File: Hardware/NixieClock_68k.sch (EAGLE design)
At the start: 47 parts, among them IC1 68008, IC10 7805, IC11 MIC803, IC12 74HC08N, IC2 AS6C1008, IC3 39SF020, IC4 DS1244Y, IC5 68681, IC6 74HC30N, IC7 74HC04N, IC8 74HC138N, IC9 74HC266N, Q1 3.6864MHz

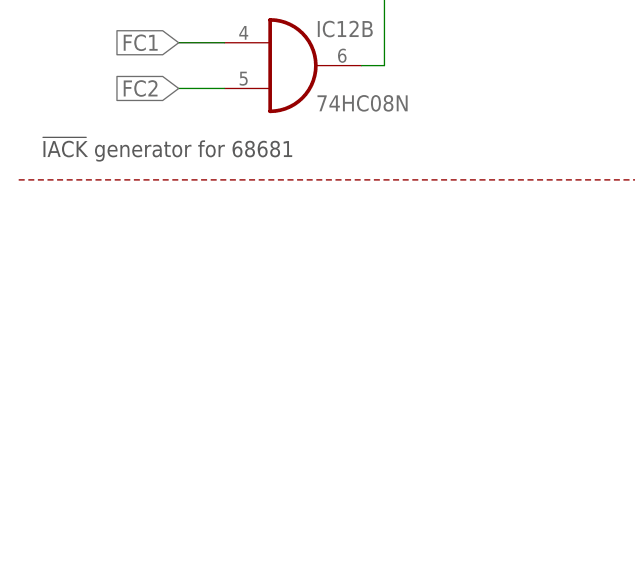
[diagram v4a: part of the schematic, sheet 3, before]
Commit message: added missing pull-ups to ROM and RAM CS; 68681 DTACK
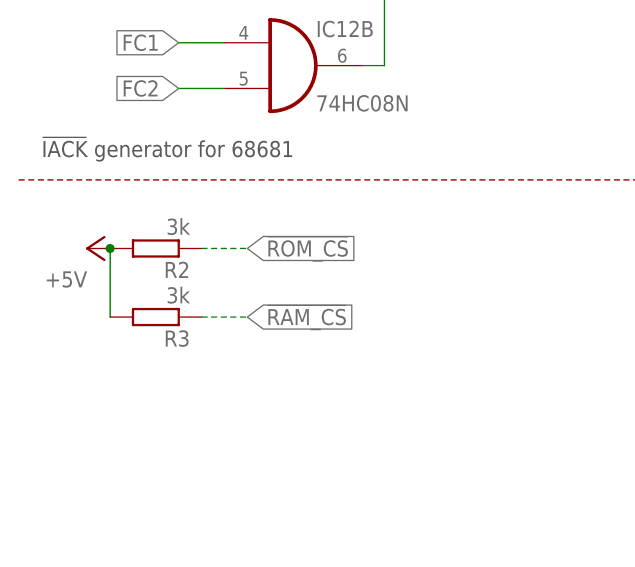
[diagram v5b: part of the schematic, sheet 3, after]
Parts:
- added R1: 10k, rcl:R-EU_R2012
- added R2, R3: 3k, rcl:R-EU_R2012
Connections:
- net !68681_DTACK: now also R1.1
- net !RAM_CS: now also R3.1
- net !ROM_CS: now also R2.1
- net +5V: now also R1.2, R2.2, R3.2
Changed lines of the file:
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@@
 <part name="P+20" library="supply1" library_urn="urn:adsk.eagle:library:371" deviceset="+5V" device=""/>
 <part name="GND13" library="supply1" library_urn="urn:adsk.eagle:library:371" deviceset="GND" device=""/>
+<part name="R1" library="rcl" library_urn="urn:adsk.eagle:library:334" deviceset="R-EU_" device="R2012" package3d_urn="urn:adsk.eagle:package:23543/2" value="10k">
+<spice>
+<pinmapping spiceprefix="R">
+<pinmap gate="G$1" pin="1" pinorder="1"/>
+<pinmap gate="G$1" pin="2" pinorder="2"/>
+</pinmapping>
+</spice>
+<attribute name="MOUSER" value="652-CR0805FX-1002ELF"/>
+</part>
+<part name="P+11" library="supply1" library_urn="urn:adsk.eagle:library:371" deviceset="+5V" device=""/>
+<part name="R2" library="rcl" library_urn="urn:adsk.eagle:library:334" deviceset="R-EU_" device="R2012" package3d_urn="urn:adsk.eagle:package:23543/2" value="3k">
+<spice>
+<pinmapping spiceprefix="R">
+<pinmap gate="G$1" pin="1" pinorder="1"/>
+<pinmap gate="G$1" pin="2" pinorder="2"/>
+</pinmapping>
+</spice>
+<attribute name="MOUSER" value="652-CR0805JW-302ELF"/>
+</part>
+<part name="P+19" library="supply1" library_urn="urn:adsk.eagle:library:371" deviceset="+5V" device=""/>
+<part name="R3" library="rcl" library_urn="urn:adsk.eagle:library:334" deviceset="R-EU_" device="R2012" package3d_urn="urn:adsk.eagle:package:23543/2" value="3k">
+<spice>
+<pinmapping spiceprefix="R">
+<pinmap gate="G$1" pin="1" pinorder="1"/>
+<pinmap gate="G$1" pin="2" pinorder="2"/>
+</pinmapping>
+</spice>
+<attribute name="MOUSER" value="652-CR0805JW-302ELF"/>
+</part>
 </parts>
 <sheets>
@@
 <attribute name="VALUE" x="30.48" y="2.54" size="1.778" layer="96"/>
 </instance>
+<instance part="R1" gate="G$1" x="40.64" y="93.98" smashed="yes" rot="R180">
+<attribute name="NAME" x="44.45" y="92.4814" size="1.778" layer="95" rot="R180"/>
+<attribute name="VALUE" x="44.45" y="97.282" size="1.778" layer="96" rot="R180"/>
+<attribute name="MOUSER" x="40.64" y="93.98" size="1.778" layer="96" rot="R180" align="top-left" display="off"/>
+</instance>
+<instance part="P+11" gate="1" x="33.02" y="93.98" smashed="yes" rot="R90">
+<attribute name="VALUE" x="33.02" y="91.44" size="1.778" layer="96" rot="R180"/>
+</instance>
 </instances>
 <busses>
-<bus name="!68681_CS,!68681_DTACK,!68681_IACK,68681_X[1..2],A[0..19],D[0..7],!IPL1,!OE,!RESET,!RTC_CS,R/!W!,STATUS[0..3],UART0_RX,UART1_TX,!VFD_RESET">
+<bus name="!68681_CS,!68681_DTACK,!68681_IACK,68681_X[1..2],A[0..19],D[0..7],!IPL1,!OE,!RTC_CS,R/!W!,STATUS[0..3],UART0_RX,UART1_TX,!VFD_RESET">
 <segment>
 <wire x1="25.4" y1="177.8" x2="68.58" y2="177.8" width="0.762" layer="92"/>
@@
 <junction x="200.66" y="134.62"/>
 </segment>
+<segment>
+<pinref part="R1" gate="G$1" pin="2"/>
+<pinref part="P+11" gate="1" pin="+5V"/>
+</segment>
 </net>
 <net name="GND" class="0">
@@
 <wire x1="30.48" y1="147.32" x2="27.94" y2="147.32" width="0.1524" layer="91"/>
 <wire x1="27.94" y1="147.32" x2="25.4" y2="149.86" width="0.1524" layer="91"/>
+</segment>
+<segment>
+<pinref part="R1" gate="G$1" pin="1"/>
+<wire x1="45.72" y1="93.98" x2="50.8" y2="93.98" width="0.1524" layer="91" style="longdash"/>
+<label x="50.8" y="93.98" size="1.778" layer="95" xref="yes"/>
 </segment>
 </net>
@@
 <attribute name="VALUE" x="76.2" y="124.46" size="1.778" layer="96"/>
 </instance>
+<instance part="R2" gate="G$1" x="15.24" y="96.52" smashed="yes" rot="R180">
+<attribute name="NAME" x="19.05" y="95.0214" size="1.778" layer="95" rot="R180"/>
+<attribute name="VALUE" x="19.05" y="99.822" size="1.778" layer="96" rot="R180"/>
+<attribute name="MOUSER" x="15.24" y="96.52" size="1.778" layer="96" rot="R180" align="top-left" display="off"/>
+</instance>
+<instance part="P+19" gate="1" x="7.62" y="96.52" smashed="yes" rot="R90">
+<attribute name="VALUE" x="7.62" y="93.98" size="1.778" layer="96" rot="R180"/>
+</instance>
+<instance part="R3" gate="G$1" x="15.24" y="88.9" smashed="yes" rot="R180">
+<attribute name="NAME" x="19.05" y="87.4014" size="1.778" layer="95" rot="R180"/>
+<attribute name="VALUE" x="19.05" y="92.202" size="1.778" layer="96" rot="R180"/>
+<attribute name="MOUSER" x="15.24" y="88.9" size="1.778" layer="96" rot="R180" align="top-left" display="off"/>
+</instance>
 </instances>
 <busses>
@@
 <pinref part="P+17" gate="1" pin="+5V"/>
 </segment>
+<segment>
+<pinref part="R2" gate="G$1" pin="2"/>
+<pinref part="P+19" gate="1" pin="+5V"/>
+<pinref part="R3" gate="G$1" pin="2"/>
+<wire x1="10.16" y1="96.52" x2="10.16" y2="88.9" width="0.1524" layer="91"/>
+<junction x="10.16" y="96.52"/>
+</segment>
 </net>
 <net name="GND" class="0">
@@
 <label x="182.88" y="58.42" size="1.778" layer="95" rot="R180" xref="yes"/>
 </segment>
+<segment>
+<pinref part="R3" gate="G$1" pin="1"/>
+<wire x1="20.32" y1="88.9" x2="25.4" y2="88.9" width="0.1524" layer="91" style="longdash"/>
+<label x="25.4" y="88.9" size="1.778" layer="95" xref="yes"/>
+</segment>
 </net>
 <net name="!ROM_CS" class="0">
@@
 <label x="182.88" y="60.96" size="1.778" layer="95" rot="R180" xref="yes"/>
 </segment>
-</net>
+<segment>
+<pinref part="R2" gate="G$1" pin="1"/>
+<wire x1="20.32" y1="96.52" x2="25.4" y2="96.52" width="0.1524" layer="91" style="longdash"/>
+<label x="25.4" y="96.52" size="1.778" layer="95" xref="yes"/>
+</segment>
+</net>

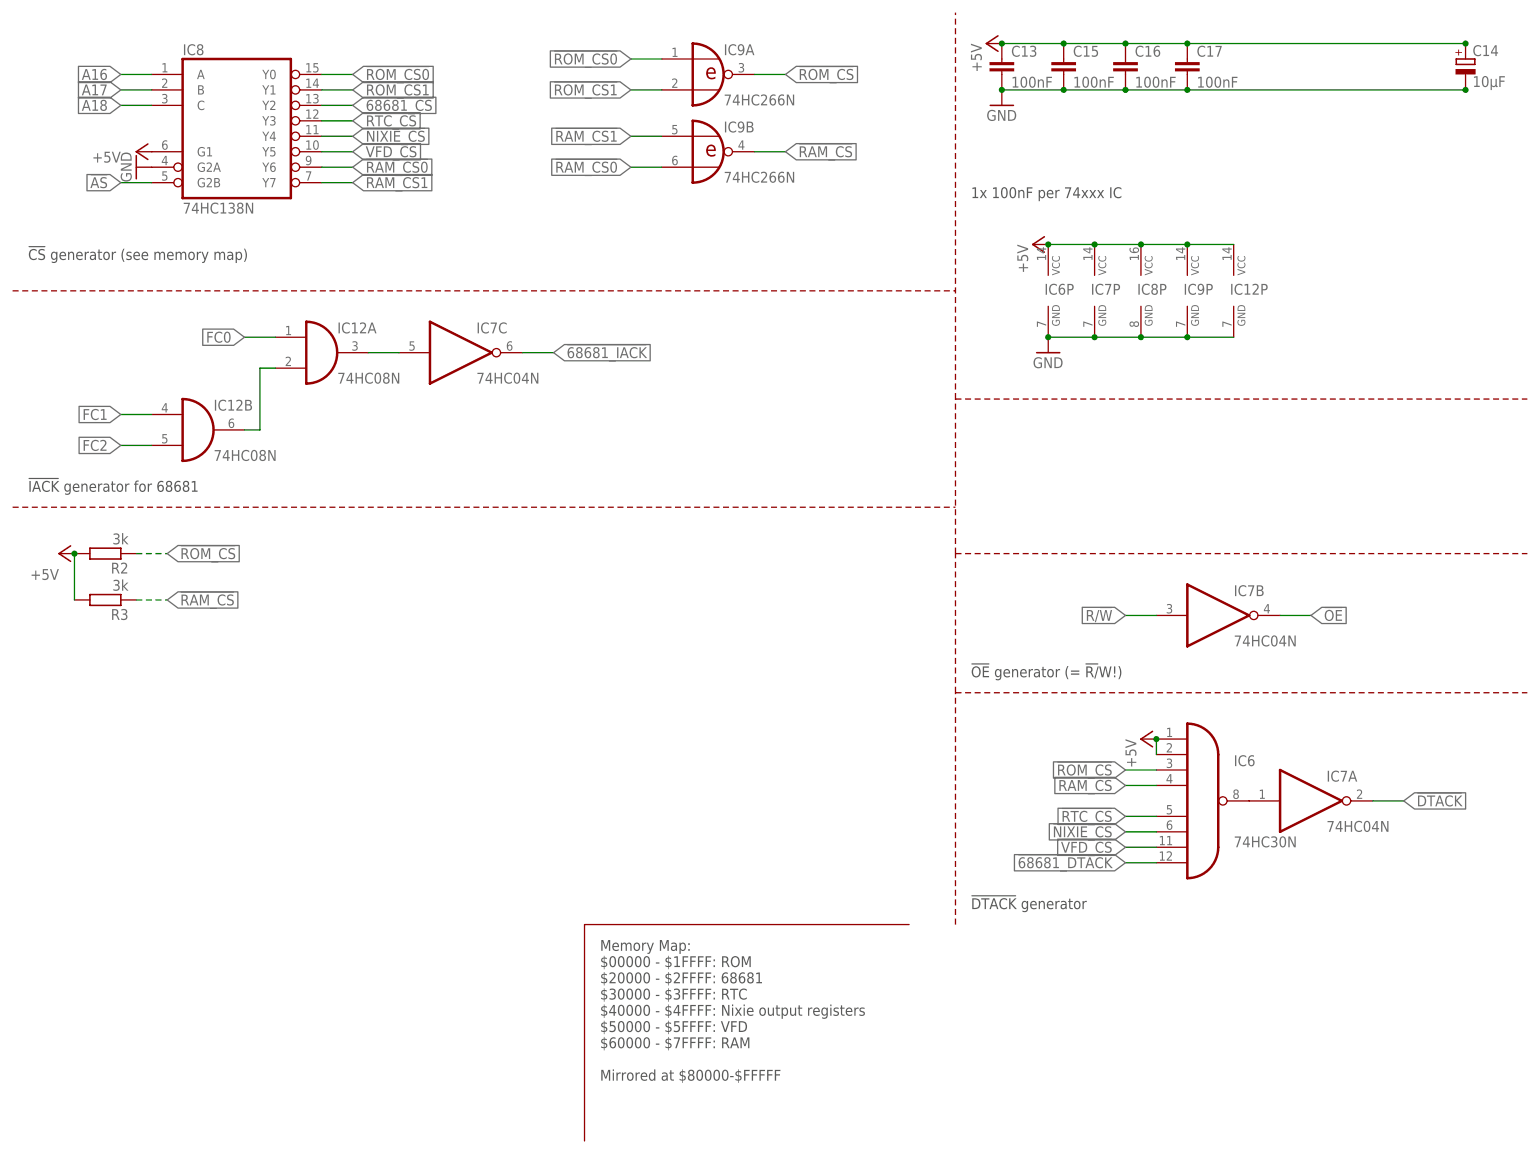
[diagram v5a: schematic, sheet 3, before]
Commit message: added data bus resistors; better reset circuit
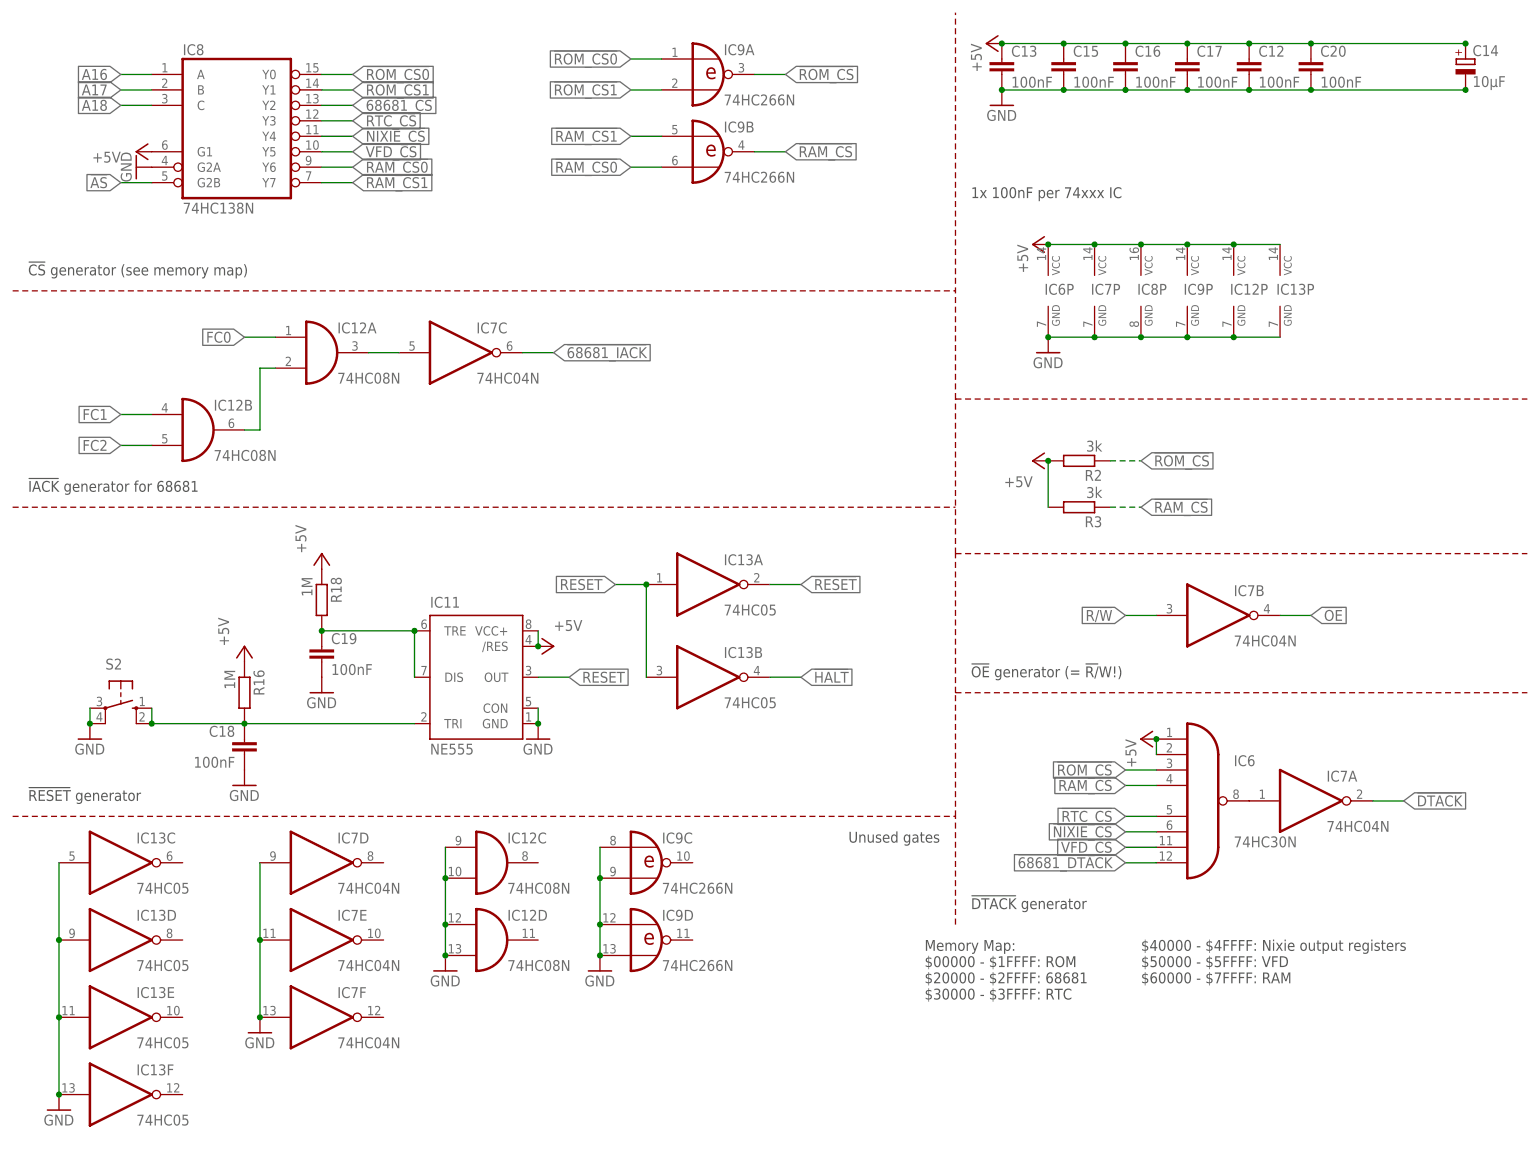
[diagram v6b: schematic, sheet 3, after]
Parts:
- removed C27: 100nF, rcl:C-EUC0805
- removed S1: (no value), switch-omron:10-XX
- added C12, C18, C19, C20: 100nF, rcl:C-EUC0805
- added IC13: 74HC05, 74xx-eu:74HCT05N
- added LED1, LED2, LED6: (no value), led:LEDCHIPLED_1206
- added R10, R11, R12, R14, R15, R17, R5, R6, R9: 10k, rcl:R-EU_R2012
- added R16, R18: 1M, rcl:R-EU_R2012
- added R19, R20, R21: 3k, rcl:R-EU_R2012
- added S2: (no value), switch-omron:10-XX
- IC11: value MIC803 -> NE555; device Parts:MIC803SOT23-3 -> st-microelectronics:NE555; MOUSER (none) -> 595-NE555P
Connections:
- new net !HALT: IC1.HALT, IC13B.O, LED2.C, R17.1
- new net N$1: C18.1, IC11.TRI, R16.2, S2.S, S2.S1
- new net N$10: LED6.A, R21.2
- new net N$12: C19.1, IC11.DIS, IC11.TRE, R18.2
- new net N$2: LED1.A, R19.2
- new net N$6: LED2.A, R20.2
- new net RESET: IC11.OUT, IC13A.I, IC13B.I
- net !DTACK: now also LED6.C
- net !RESET: now also IC13A.O, LED1.C; no longer IC1.HALT, IC11.!RESET, S1.S, S1.S1
- net +5V: now also C12.1, C20.1, IC11./RES, IC11.VCC+, IC13P.VCC, R16.1, R17.2, R18.1, R19.1, R20.1, R21.1; no longer C27.1, IC11.VCC
- net D0: now also R5.2
- net D1: now also R6.2
- net D2: now also R9.2
- net D3: now also R10.2
- net D4: now also R11.2
- net D5: now also R12.2
- net D6: now also R14.2
- net D7: now also R15.2
- net GND: now also C12.2, C18.2, C19.2, C20.2, IC11.CON, IC12C.I0, IC12C.I1, IC12D.I0, IC12D.I1, IC13C.I, IC13D.I, IC13E.I, IC13F.I, IC13P.GND, IC7D.I, IC7E.I, IC7F.I, IC9C.I0, IC9C.I1, IC9D.I0, IC9D.I1, R10.1, R11.1, R12.1, R14.1, R15.1, R5.1, R6.1, R9.1, S2.P, S2.P1; no longer C27.2, S1.P, S1.P1
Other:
- note added: "!RESET! generator"
- note added: "$40000 - $4FFFF: Nixie output registers $50000 - $5FFFF: VFD $60000 - $7FFFF: RAM"
- note added: "Memory Map: $00000 - $1FFFF: ROM $20000 - $2FFFF: 68681 $30000 - $3FFFF: RTC"
- note added: "Unused gates"
- note removed: "Memory Map: $00000 - $1FFFF: ROM $20000 - $2FFFF: 68681 $30000 - $3FFFF: RTC $40000 - $4FFFF: Nixie output registers $50000 - $5FFFF: VFD $60000 - $7FFFF: RAM Mirrored at $80000-$FFFFF"
- moved on the sheet: R2, R3

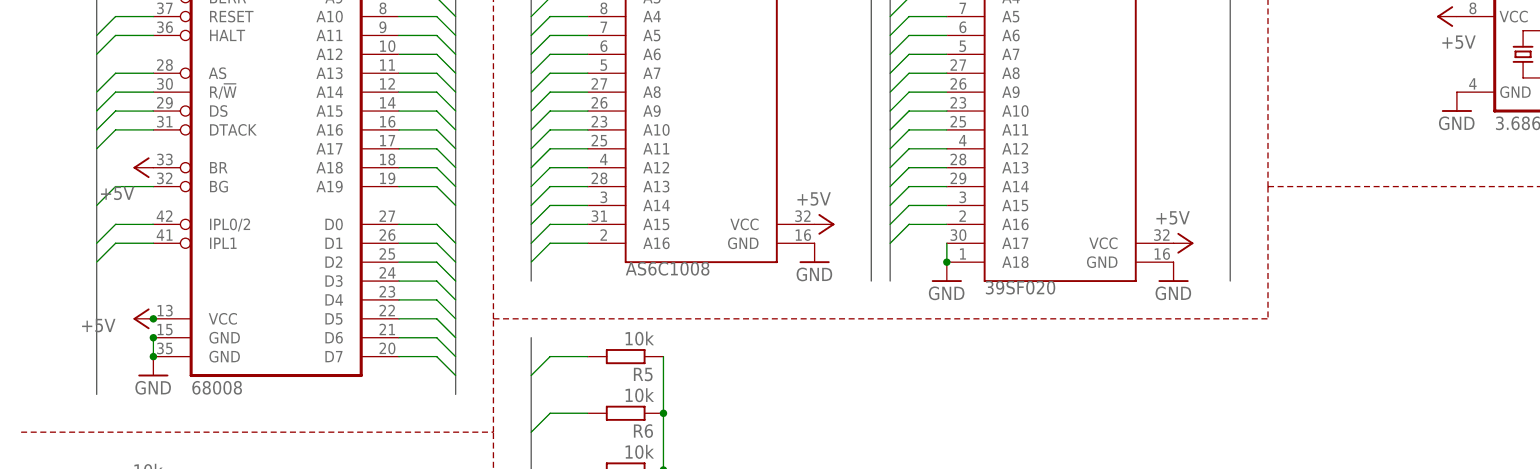
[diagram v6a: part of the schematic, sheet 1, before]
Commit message: basic 68681 initialization; more nixie driver routines and ram defines
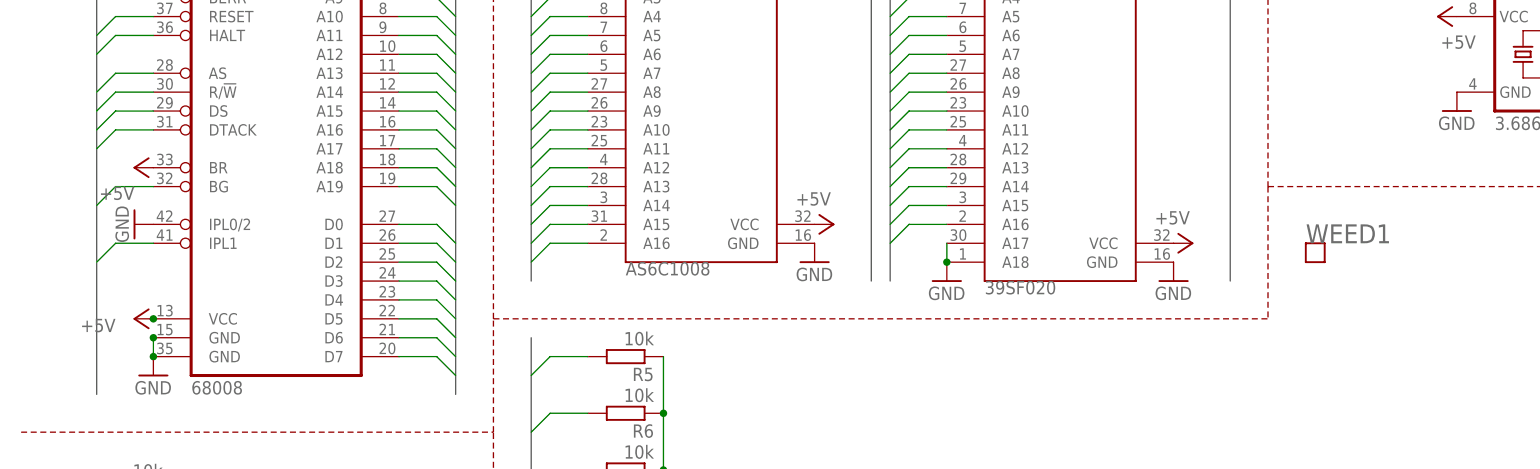
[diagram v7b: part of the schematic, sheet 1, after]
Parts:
- added WEED1: WEED, Parts:WEED
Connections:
- removed net !IPL0/2: IC1.IPL0/2
- net GND: now also IC1.IPL0/2
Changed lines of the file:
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@@
 <attribute name="MOUSER" value="710-156120VS75300"/>
 </part>
+<part name="WEED1" library="Parts" deviceset="WEED" device=""/>
+<part name="GND33" library="supply1" library_urn="urn:adsk.eagle:library:371" deviceset="GND" device=""/>
 </parts>
 <sheets>
@@
 <attribute name="MOUSER" x="22.86" y="43.18" size="1.778" layer="96" rot="R90" align="top-left" display="off"/>
 </instance>
+<instance part="WEED1" gate="G$1" x="172.72" y="111.76" smashed="yes">
+<attribute name="NAME" x="172.72" y="114.3" size="2.54" layer="95" font="vector"/>
+</instance>
+<instance part="GND33" gate="1" x="15.24" y="116.84" smashed="yes" rot="R270">
+<attribute name="VALUE" x="12.7" y="119.38" size="1.778" layer="96" rot="R270"/>
+</instance>
 </instances>
 <busses>
@@
 <junction x="86.36" y="45.72"/>
 </segment>
+<segment>
+<pinref part="IC1" gate="G$1" pin="IPL0/2"/>
+<pinref part="GND33" gate="1" pin="GND"/>
+</segment>
 </net>
 <net name="CLK" class="0">
@@
 </segment>
 </net>
-<net name="!IPL0/2" class="0">
-<segment>
-<pinref part="IC1" gate="G$1" pin="IPL0/2"/>
-<wire x1="17.78" y1="116.84" x2="12.7" y2="116.84" width="0.1524" layer="91"/>
-<wire x1="12.7" y1="116.84" x2="10.16" y2="114.3" width="0.1524" layer="91"/>
-</segment>
-</net>
